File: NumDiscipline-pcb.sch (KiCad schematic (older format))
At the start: 190 parts, among them J1 AVR-ISP-6, SW1 KEYSW, SW10 KEYSW, SW11 KEYSW, SW12 KEYSW, SW13 KEYSW, SW14 KEYSW, SW15 KEYSW, SW16 KEYSW, SW17 KEYSW, SW18 KEYSW, SW19 KEYSW, SW2 KEYSW, SW20 KEYSW, SW21 KEYSW, SW22 KEYSW, SW23 KEYSW, SW24 KEYSW, SW25 KEYSW, SW26 KEYSW, SW27 KEYSW, SW28 KEYSW, SW29 KEYSW, SW3 KEYSW, SW30 KEYSW, SW31 KEYSW, SW32 KEYSW, SW33 KEYSW, SW34 KEYSW, SW35 KEYSW, SW36 KEYSW, SW37 KEYSW, SW38 KEYSW, SW39 KEYSW, SW4 KEYSW, SW40 KEYSW, SW41 KEYSW, SW42 KEYSW, SW43 KEYSW, SW44 KEYSW, SW45 KEYSW, SW46 KEYSW, SW47 KEYSW, SW48 KEYSW, SW49 KEYSW, SW5 KEYSW, SW50 KEYSW, SW51 KEYSW, SW52 KEYSW, SW53 KEYSW, SW54 KEYSW, SW55 KEYSW, SW56 KEYSW, SW57 KEYSW, SW58 KEYSW, SW59 KEYSW, SW6 KEYSW, SW60 KEYSW, SW61 KEYSW, SW62 KEYSW, SW63 KEYSW, SW64 KEYSW, SW65 KEYSW, SW66 KEYSW, SW67 KEYSW, SW68 KEYSW, SW69 KEYSW, SW7 KEYSW, SW70 KEYSW, SW71 KEYSW, SW72 KEYSW, SW73 KEYSW, SW74 KEYSW, SW75 KEYSW, SW76 KEYSW, SW77 KEYSW, SW78 KEYSW, SW79 KEYSW, SW8 KEYSW, SW80 KEYSW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

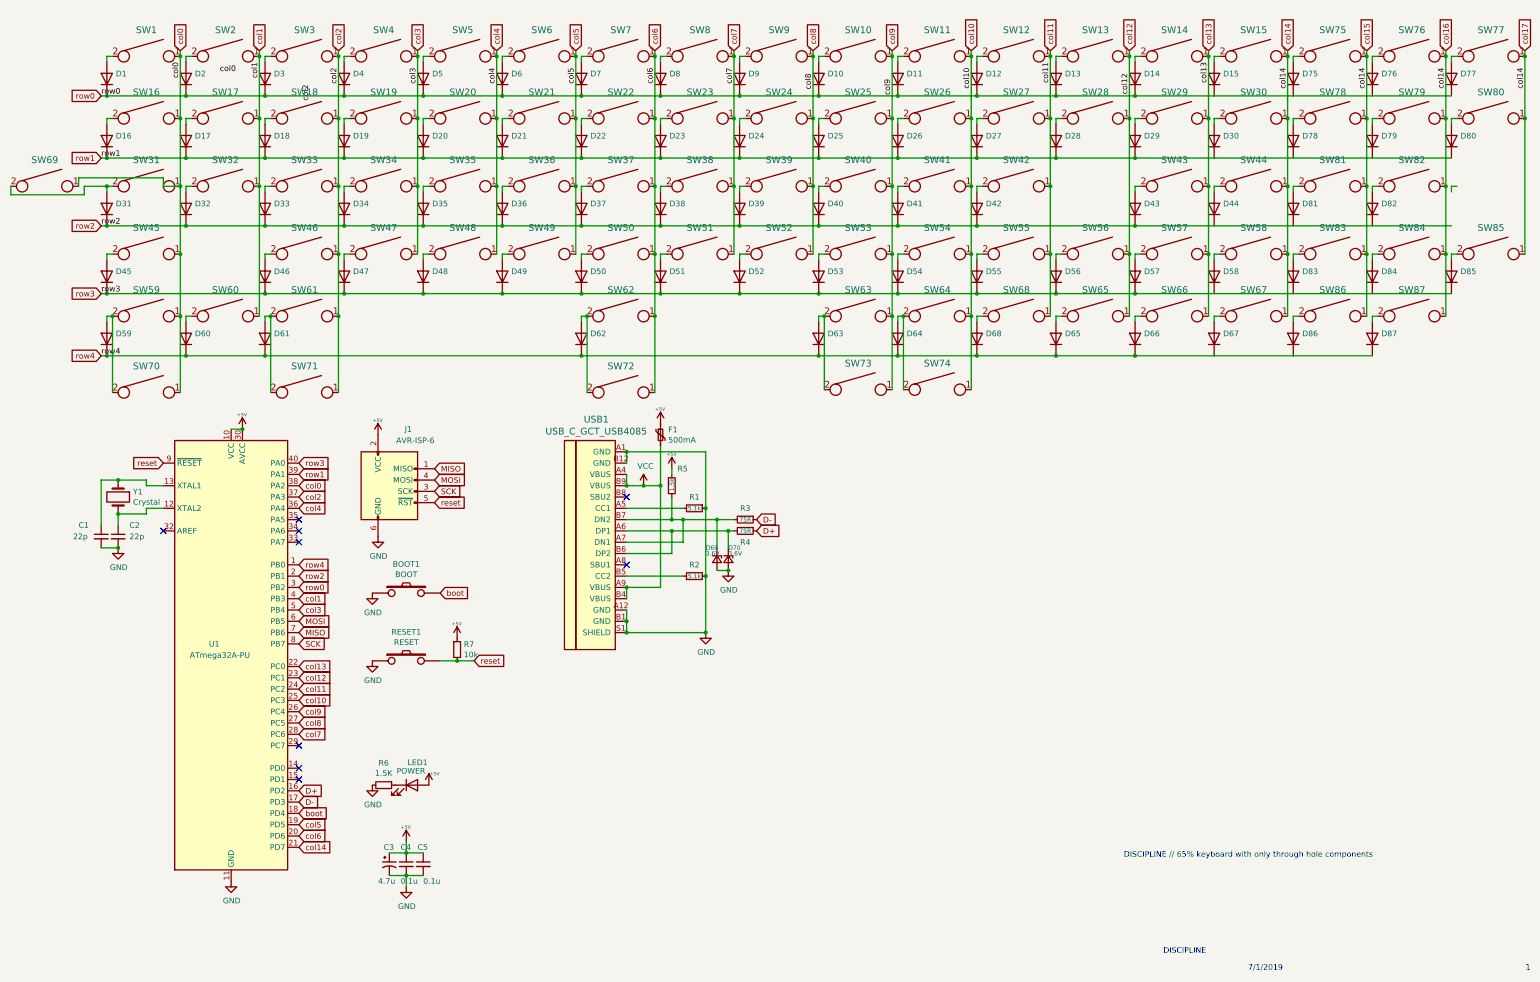
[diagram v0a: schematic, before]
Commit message: working on routing, renamed project file
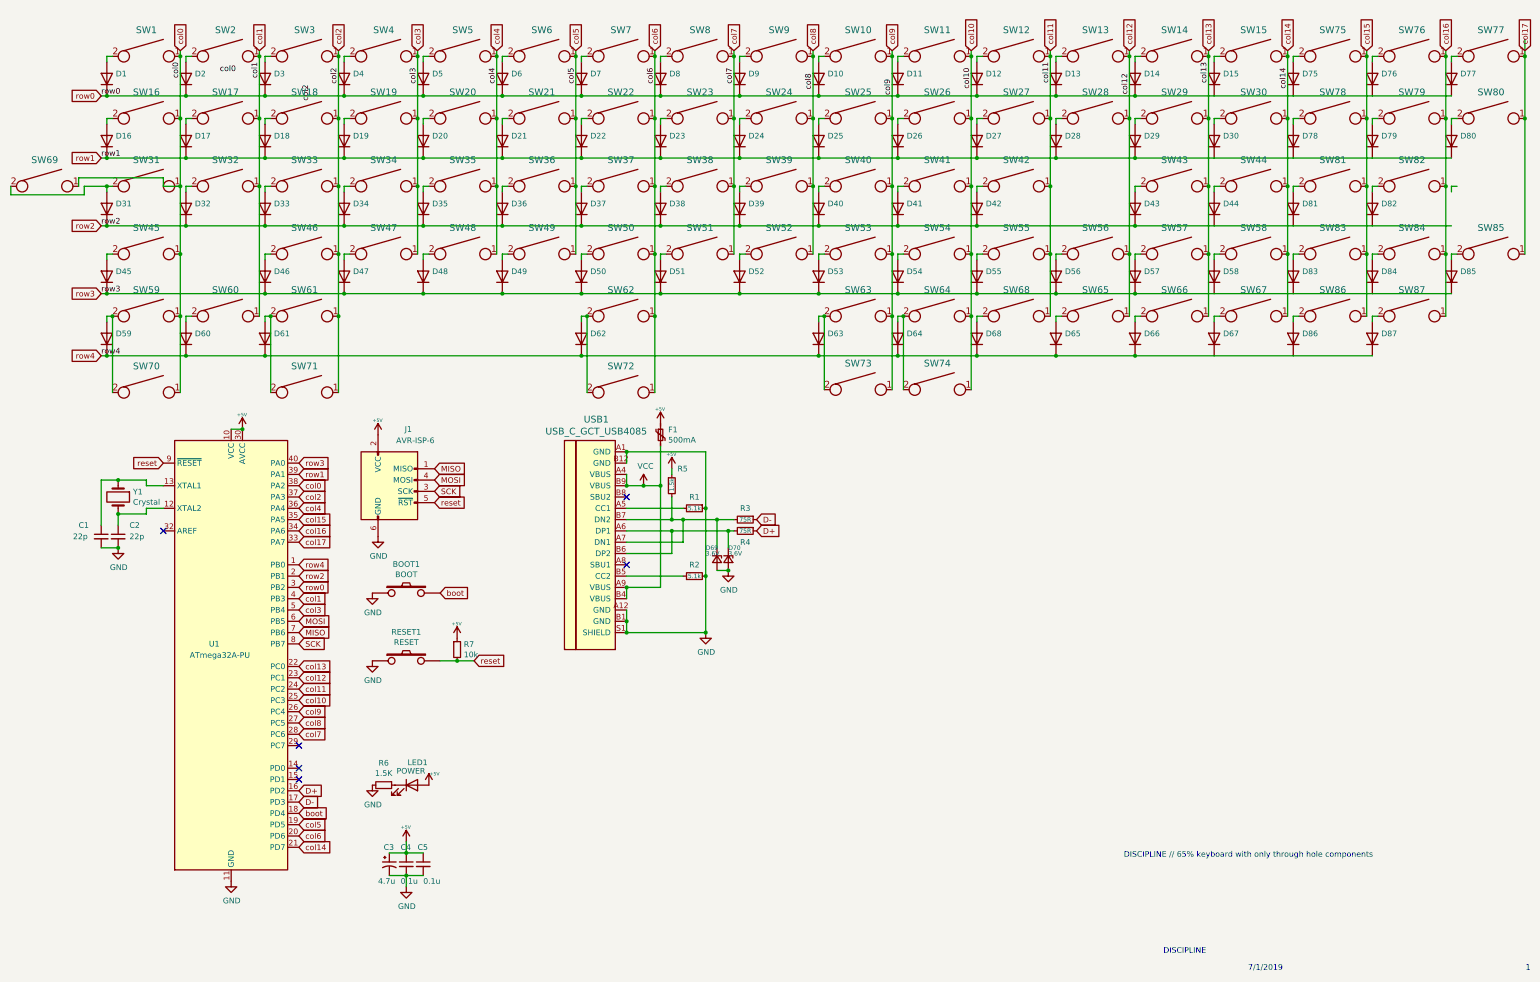
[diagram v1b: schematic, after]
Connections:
- net col14: no longer SW75.1, SW76.1, SW77.1, SW78.1, SW79.1, SW80.1, SW81.1, SW82.1, SW83.1, SW84.1, SW85.1, SW86.1, SW87.1
- net col17: now reaches U1.33 (PA7)
- net col17: now also SW77.1, SW80.1, SW85.1
- net col16: now reaches U1.34 (PA6)
- net col16: now also SW76.1, SW79.1, SW82.1, SW84.1, SW87.1
- net col15: now reaches U1.35 (PA5)
- net col15: now also SW75.1, SW78.1, SW81.1, SW83.1, SW86.1
- no-connect marks 9 -> 6

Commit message: add plate
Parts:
- added J2, J3: MOLEX_39-53-2304, MOLEX_39-53-2304:MOLEX_39-53-2304_0, symbol MOLEX_39-53-2304:MOLEX_39-53-2304
- SW1: value KEYSW -> ESCAPE
- SW2: value KEYSW -> 1
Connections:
- net col0: now also J2.6, J3.6
- net col1: now also J2.7, J3.7
- net col10: now also J2.16, J3.16
- net col11: now also J2.17, J3.17
- net col12: now also J2.18, J3.18
- net col13: now also J2.19, J3.19
- net col14: now also J2.20, J3.20
- net col15: now also J2.21, J3.21
- net col16: now also J2.22, J3.22
- net col17: now also J2.23, J3.23
- net col2: now also J2.8, J3.8
- net col3: now also J2.9, J3.9
- net col4: now also J2.10, J3.10
- net col5: now also J2.11, J3.11
- net col6: now also J2.12, J3.12
- net col7: now also J2.13, J3.13
- net col8: now also J2.14, J3.14
- net col9: now also J2.15, J3.15
- net row0: now also J2.1, J3.1
- net row1: now also J2.2, J3.2
- net row2: now also J2.3, J3.3
- net row3: now also J2.4, J3.4
- net row4: now also J2.5, J3.5

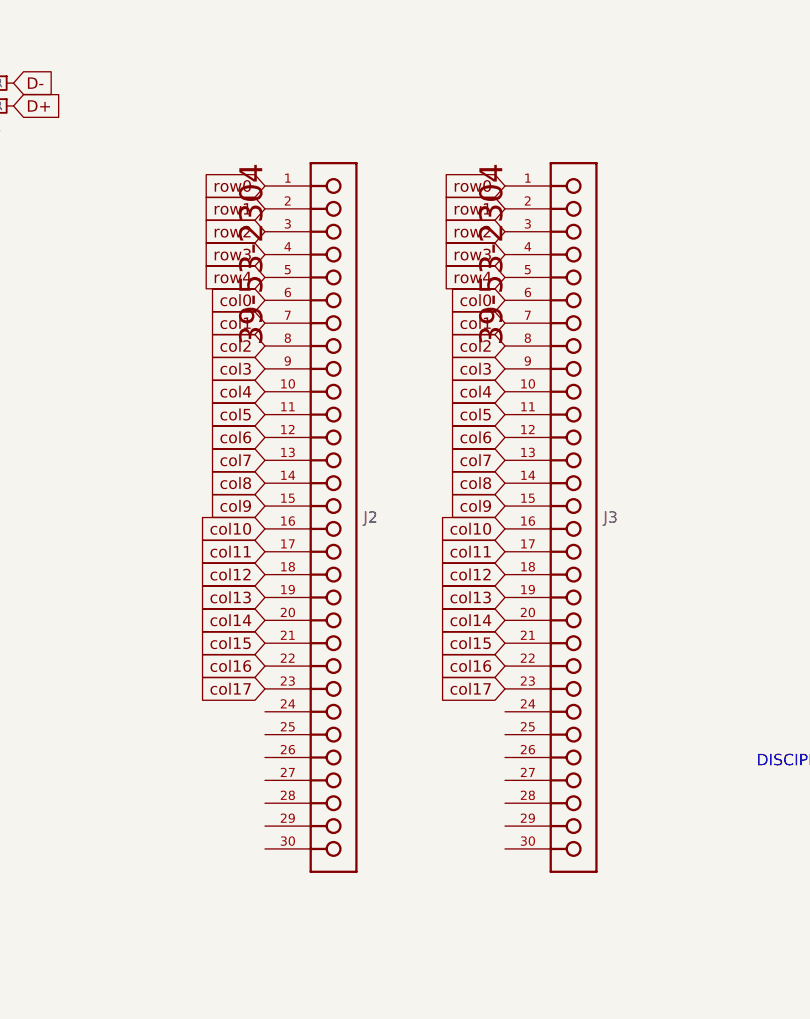
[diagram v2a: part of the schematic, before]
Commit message: add 3d, finish plate
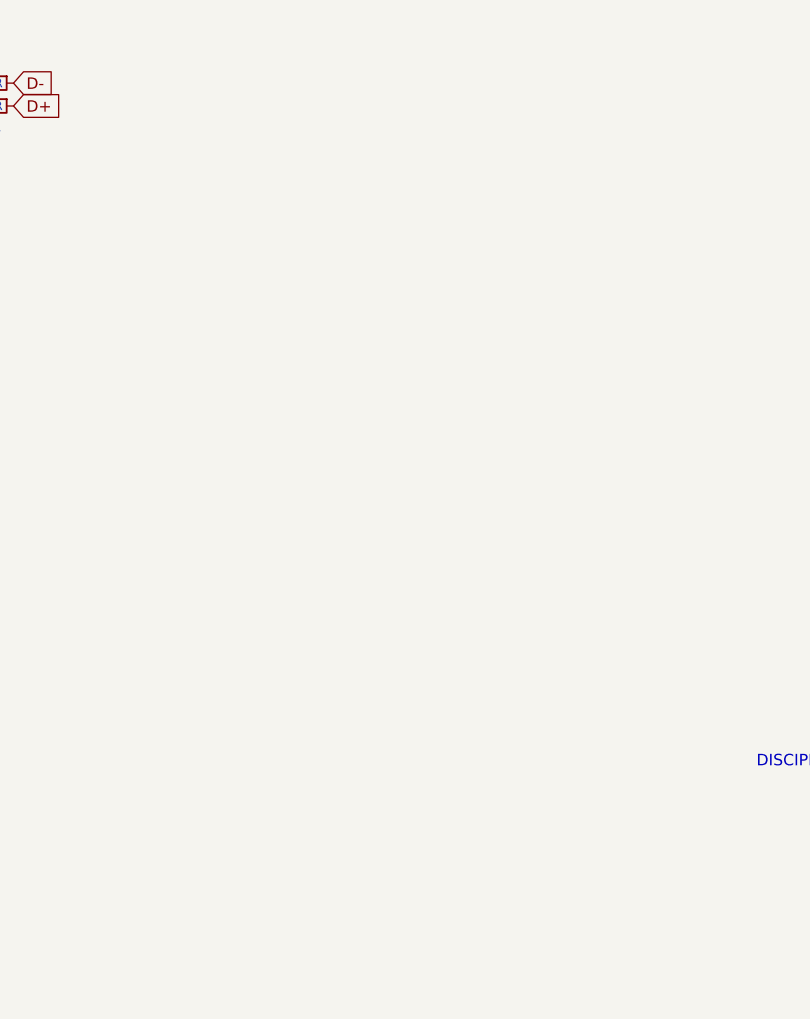
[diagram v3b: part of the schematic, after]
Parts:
- removed J2, J3: MOLEX_39-53-2304, MOLEX_39-53-2304:MOLEX_39-53-2304_0, symbol MOLEX_39-53-2304:MOLEX_39-53-2304
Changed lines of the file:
@@
 	0    -1   -1   0
 $EndComp
-Text GLabel 9750 7500 0    50   Input ~ 0
-row0
-Text GLabel 9750 7600 0    50   Input ~ 0
-row1
-Text GLabel 9750 7700 0    50   Input ~ 0
-row2
-Text GLabel 9750 7800 0    50   Input ~ 0
-row3
-Text GLabel 9750 7900 0    50   Input ~ 0
-row4
-Text GLabel 9750 8000 0    50   Input ~ 0
-col0
-Text GLabel 9750 8100 0    50   Input ~ 0
-col1
-Text GLabel 9750 8200 0    50   Input ~ 0
-col2
-Text GLabel 9750 8300 0    50   Input ~ 0
-col3
-Text GLabel 9750 8400 0    50   Input ~ 0
-col4
-Text GLabel 9750 8500 0    50   Input ~ 0
-col5
-Text GLabel 9750 8600 0    50   Input ~ 0
-col6
-Text GLabel 9750 8700 0    50   Input ~ 0
-col7
-Text GLabel 9750 8800 0    50   Input ~ 0
-col8
-Text GLabel 9750 8900 0    50   Input ~ 0
-col9
-Text GLabel 9750 9000 0    50   Input ~ 0
-col10
-Text GLabel 9750 9100 0    50   Input ~ 0
-col11
-Text GLabel 9750 9200 0    50   Input ~ 0
-col12
-Text GLabel 9750 9300 0    50   Input ~ 0
-col13
-Text GLabel 9750 9400 0    50   Input ~ 0
-col14
-Text GLabel 9750 9500 0    50   Input ~ 0
-col15
-Text GLabel 9750 9600 0    50   Input ~ 0
-col16
-Text GLabel 9750 9700 0    50   Input ~ 0
-col17
-$Comp
-L MOLEX_39-53-2304:MOLEX_39-53-2304 J2
-U 1 1 5ECCC4D7
-P 10350 7400
-F 0 "J2" V 11900 7230 50  0000 L CNN
-F 1 "MOLEX_39-53-2304" H 10350 7400 50  0001 L BNN
-F 2 "MOLEX_39-53-2304:MOLEX_39-53-2304_0" H 10350 7400 50  0001 L BNN
-F 3 "" H 10350 7400 50  0001 C CNN
-	1    10350 7400
-	0    1    1    0
-$EndComp
-Text GLabel 10800 7500 0    50   Input ~ 0
-row0
-Text GLabel 10800 7600 0    50   Input ~ 0
-row1
-Text GLabel 10800 7700 0    50   Input ~ 0
-row2
-Text GLabel 10800 7800 0    50   Input ~ 0
-row3
-Text GLabel 10800 7900 0    50   Input ~ 0
-row4
-Text GLabel 10800 8000 0    50   Input ~ 0
-col0
-Text GLabel 10800 8100 0    50   Input ~ 0
-col1
-Text GLabel 10800 8200 0    50   Input ~ 0
-col2
-Text GLabel 10800 8300 0    50   Input ~ 0
-col3
-Text GLabel 10800 8400 0    50   Input ~ 0
-col4
-Text GLabel 10800 8500 0    50   Input ~ 0
-col5
-Text GLabel 10800 8600 0    50   Input ~ 0
-col6
-Text GLabel 10800 8700 0    50   Input ~ 0
-col7
-Text GLabel 10800 8800 0    50   Input ~ 0
-col8
-Text GLabel 10800 8900 0    50   Input ~ 0
-col9
-Text GLabel 10800 9000 0    50   Input ~ 0
-col10
-Text GLabel 10800 9100 0    50   Input ~ 0
-col11
-Text GLabel 10800 9200 0    50   Input ~ 0
-col12
-Text GLabel 10800 9300 0    50   Input ~ 0
-col13
-Text GLabel 10800 9400 0    50   Input ~ 0
-col14
-Text GLabel 10800 9500 0    50   Input ~ 0
-col15
-Text GLabel 10800 9600 0    50   Input ~ 0
-col16
-Text GLabel 10800 9700 0    50   Input ~ 0
-col17
-$Comp
-L MOLEX_39-53-2304:MOLEX_39-53-2304 J3
-U 1 1 5ED45368
-P 11400 7400
-F 0 "J3" V 12950 7230 50  0000 L CNN
-F 1 "MOLEX_39-53-2304" H 11400 7400 50  0001 L BNN
-F 2 "MOLEX_39-53-2304:MOLEX_39-53-2304_0" H 11400 7400 50  0001 L BNN
-F 3 "" H 11400 7400 50  0001 C CNN
-	1    11400 7400
-	0    1    1    0
-$EndComp
 $EndSCHEMATC

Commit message: start making adjustments from first proto
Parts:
- BOOT1, RESET1: symbol discipline-pcb-rescue:SW_PUSH-keyboard_parts -> NumDiscipline-pcb-rescue:SW_PUSH-keyboard_parts-discipline-pcb-rescue
- C4, C5: footprint cftkb:D_DO-35_SOD27_P5.08mm_Horizontal -> cftkb:C_Disc_D4.3mm_W1.9mm_P5.00mm
- J1: symbol discipline-pcb-rescue:AVR-ISP-6-Connector -> NumDiscipline-pcb-rescue:AVR-ISP-6-Connector-discipline-pcb-rescue
- SW1, SW10, SW11, SW12, SW13, SW14, SW15, SW16, SW17, SW18, SW19, SW2, SW20, SW21, SW22, SW23, SW24, SW25, SW26, SW27, SW28, SW29, SW3, SW30, SW31, SW32, SW33, SW34, SW35, SW36, SW37, SW38, SW39, SW4, SW40, SW41, SW42, SW43, SW44, SW45, SW46, SW47, SW48, SW49, SW5, SW50, SW51, SW52, SW53, SW54, SW55, SW56, SW57, SW58, SW59, SW6, SW60, SW61, SW62, SW63, SW64, SW65, SW66, SW67, SW68, SW69, SW7, SW70, SW71, SW72, SW73, SW74, SW75, SW76, SW77, SW78, SW79, SW8, SW80, SW81, SW82, SW83, SW84, SW85, SW86, SW87, SW9: symbol discipline-pcb-rescue:KEYSW-keyboard_parts -> NumDiscipline-pcb-rescue:KEYSW-keyboard_parts-discipline-pcb-rescue
- U1: symbol discipline-pcb-rescue:ATmega32A-PU-MCU_Microchip_ATmega -> NumDiscipline-pcb-rescue:ATmega32A-PU-MCU_Microchip_ATmega-discipline-pcb-rescue
- USB1: symbol discipline-pcb-rescue:USB_C_GCT_USB4085-Type-C -> NumDiscipline-pcb-rescue:USB_C_GCT_USB4085-Type-C-discipline-pcb-rescue
